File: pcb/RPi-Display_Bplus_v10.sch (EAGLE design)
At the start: 56 parts, among them IC1 ADS7846, IC2 24LC-I/OT, Q1 N-CHN, SW1 SWITCH-PTS840P, SW2 SWITCH-PTS840P, SW3 SWITCH-PTS840P, U1 TS5204-3V3, X1 PASSER, X2 PASSER, X3 PASSER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

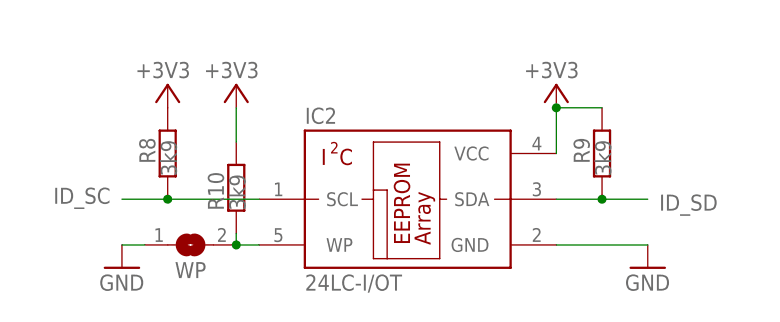
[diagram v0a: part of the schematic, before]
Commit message: updated schematics
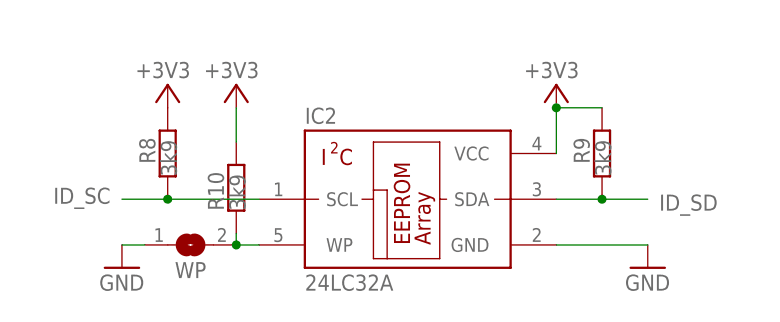
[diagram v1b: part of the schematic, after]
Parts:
- IC2: value 24LC-I/OT -> 24LC32A
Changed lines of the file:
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@@
 <part name="+3V6" library="supply1" deviceset="+3V3" device=""/>
 <part name="+3V9" library="supply1" deviceset="+3V3" device=""/>
-<part name="IC2" library="we-chip" deviceset="I2C_EEPROM" device="-CAT24AA0X" value="24LC-I/OT"/>
+<part name="IC2" library="we-chip" deviceset="I2C_EEPROM" device="-CAT24AA0X" value="24LC32A"/>
 <part name="R8" library="rcl" deviceset="R-EU_" device="R0603" value="3k9"/>
 <part name="R9" library="rcl" deviceset="R-EU_" device="R0603" value="3k9"/>

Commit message: cleaned up schematics and layout
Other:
- note removed: "www.watterott.com"
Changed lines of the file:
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@@
 <setting verticaltext="up"/>
 </settings>
-<grid distance="0.1" unitdist="inch" unit="inch" style="lines" multiple="1" display="no" altdistance="0.01" altunitdist="inch" altunit="inch"/>
+<grid distance="0.05" unitdist="inch" unit="inch" style="lines" multiple="1" display="yes" altdistance="0.025" altunitdist="inch" altunit="inch"/>
 <layers>
 <layer number="1" name="Top" color="4" fill="1" visible="no" active="no"/>
@@
 <part name="U$1" library="welectronic" deviceset="WE-LOGO" device="PLACE" value="WE-LOGO"/>
 <part name="LOGO1" library="OSHW" deviceset="OSHW_LOGO_6MIL" device="X0150-NT"/>
-<part name="FRAME1" library="frames" deviceset="A4L-LOC" device=""/>
 <part name="R1" library="rcl" deviceset="R-EU_" device="R0603" value="47"/>
 <part name="R2" library="rcl" deviceset="R-EU_" device="R0603" value="47"/>
@@
 <part name="SW3" library="we-switch" deviceset="SWITCH" device="-PTS840P"/>
 <part name="GND7" library="supply1" deviceset="GND" device=""/>
+<part name="FRAME1" library="we-symbol" deviceset="FRAME-A4L" device=""/>
 </parts>
 <sheets>
@@
 <text x="31.75" y="167.64" size="3.81" layer="250">2.8" Display with Touchpanel</text>
 <text x="198.12" y="167.64" size="3.81" layer="250">Raspberry Pi B+</text>
-<text x="161.29" y="31.75" size="1.27" layer="95">Released under the Creative Commons Attribution Share-Alike License</text>
-<text x="161.29" y="29.21" size="1.27" layer="95">http://creativecommons.org/licenses/by-sa/4.0/</text>
-<text x="161.29" y="25.4" size="1.27" layer="95">Designed by Andreas Watterott (Watterott electronic)</text>
+<text x="162.56" y="21.59" size="1.27" layer="95">Released under the Creative Commons Attribution Share-Alike License</text>
+<text x="162.56" y="19.05" size="1.27" layer="95">http://creativecommons.org/licenses/by-sa/4.0/</text>
+<text x="162.56" y="15.24" size="1.27" layer="95">Designed by Andreas Watterott (Watterott electronic)</text>
 <text x="115.57" y="105.41" size="3.81" layer="250">Touch Controller</text>
 <text x="127" y="64.77" size="1.778" layer="95">or TSC2046</text>
@@
 <text x="52.705" y="142.875" size="1.27" layer="250" font="vector">1</text>
 <text x="52.705" y="140.335" size="1.27" layer="250" font="vector">1</text>
-<text x="213.36" y="5.08" size="2.54" layer="94" font="vector" align="bottom-right">www.watterott.com</text>
 <text x="125.73" y="161.29" size="3.81" layer="250">Switches</text>
 </plain>
@@
 <attribute name="VALUE" x="107.315" y="7.62" size="1.778" layer="96"/>
 </instance>
-<instance part="X1" gate="G$1" x="167.64" y="19.05"/>
-<instance part="X2" gate="G$1" x="175.26" y="19.05"/>
-<instance part="X3" gate="G$1" x="182.88" y="19.05"/>
-<instance part="X4" gate="G$1" x="190.5" y="19.05"/>
-<instance part="U$1" gate="G$1" x="207.01" y="19.05"/>
-<instance part="LOGO1" gate="G$1" x="207.01" y="11.43"/>
-<instance part="FRAME1" gate="G$1" x="0" y="0" smashed="yes">
-<attribute name="DRAWING_NAME" x="217.17" y="15.24" size="2.54" layer="94" font="vector"/>
-<attribute name="LAST_DATE_TIME" x="217.17" y="10.16" size="2.286" layer="94" font="vector"/>
-<attribute name="SHEET" x="230.505" y="5.08" size="2.54" layer="94" font="vector"/>
-</instance>
+<instance part="X1" gate="G$1" x="165.1" y="7.62"/>
+<instance part="X2" gate="G$1" x="170.18" y="7.62"/>
+<instance part="X3" gate="G$1" x="175.26" y="7.62"/>
+<instance part="X4" gate="G$1" x="180.34" y="7.62"/>
+<instance part="U$1" gate="G$1" x="208.28" y="7.62"/>
+<instance part="LOGO1" gate="G$1" x="198.12" y="7.62"/>
 <instance part="R1" gate="G$1" x="87.63" y="115.57" smashed="yes">
 <attribute name="NAME" x="80.01" y="115.7986" size="1.778" layer="95"/>
@@
 <attribute name="VALUE" x="192.405" y="77.47" size="1.778" layer="96" rot="R180"/>
 </instance>
-<instance part="LOGO2" gate="G$1" x="191.77" y="11.43"/>
+<instance part="LOGO2" gate="G$1" x="187.96" y="7.62"/>
 <instance part="RPI" gate="RPI" x="215.9" y="134.62"/>
 <instance part="GPIO" gate="-1" x="231.14" y="109.22" smashed="yes" rot="R180"/>
@@
 <attribute name="VALUE" x="124.46" y="120.65" size="1.778" layer="96"/>
 </instance>
+<instance part="FRAME1" gate="G$1" x="0" y="0"/>
 </instances>
 <busses>
